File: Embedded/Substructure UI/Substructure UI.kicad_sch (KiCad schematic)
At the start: 6 parts, among them J1 Conn_01x04_Socket, J2 Conn_01x04_Socket, U2 TLV74133PDBVR

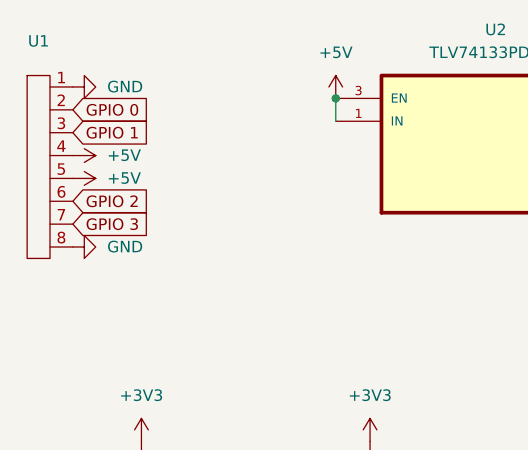
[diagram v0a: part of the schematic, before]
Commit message: Modified Ports to fit FFC orientations
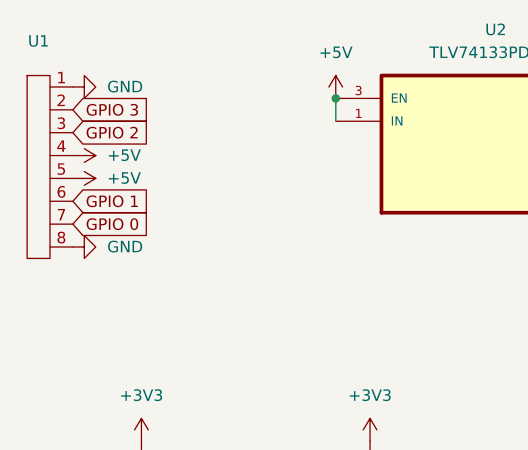
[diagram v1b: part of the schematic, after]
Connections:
- net GPIO 0: now also U1.7; no longer U1.2
- net GPIO 1: now also U1.6; no longer U1.3
- net GPIO 2: now also U1.3; no longer U1.6
- net GPIO 3: now also U1.2; no longer U1.7
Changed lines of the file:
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@@
 	(global_label "GPIO 2"
 		(shape input)
-		(at 30.48 52.07 0)
+		(at 30.48 44.45 0)
 		(fields_autoplaced yes)
 		(effects
@@
 		)
 		(property "Intersheetrefs" "${INTERSHEET_REFS}"
-			(at 40.1176 52.07 0)
+			(at 40.1176 44.45 0)
 			(effects
 				(font
@@
 	(global_label "GPIO 3"
 		(shape input)
-		(at 30.48 54.61 0)
+		(at 30.48 41.91 0)
 		(fields_autoplaced yes)
 		(effects
@@
 		)
 		(property "Intersheetrefs" "${INTERSHEET_REFS}"
-			(at 40.1176 54.61 0)
+			(at 40.1176 41.91 0)
 			(effects
 				(font
@@
 	(global_label "GPIO 0"
 		(shape input)
-		(at 30.48 41.91 0)
+		(at 30.48 54.61 0)
 		(fields_autoplaced yes)
 		(effects
@@
 		)
 		(property "Intersheetrefs" "${INTERSHEET_REFS}"
-			(at 40.1176 41.91 0)
+			(at 40.1176 54.61 0)
 			(effects
 				(font
@@
 	(global_label "GPIO 1"
 		(shape input)
-		(at 30.48 44.45 0)
+		(at 30.48 52.07 0)
 		(fields_autoplaced yes)
 		(effects
@@
 		)
 		(property "Intersheetrefs" "${INTERSHEET_REFS}"
-			(at 40.1176 44.45 0)
+			(at 40.1176 52.07 0)
 			(effects
 				(font
